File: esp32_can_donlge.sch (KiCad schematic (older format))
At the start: 0 parts

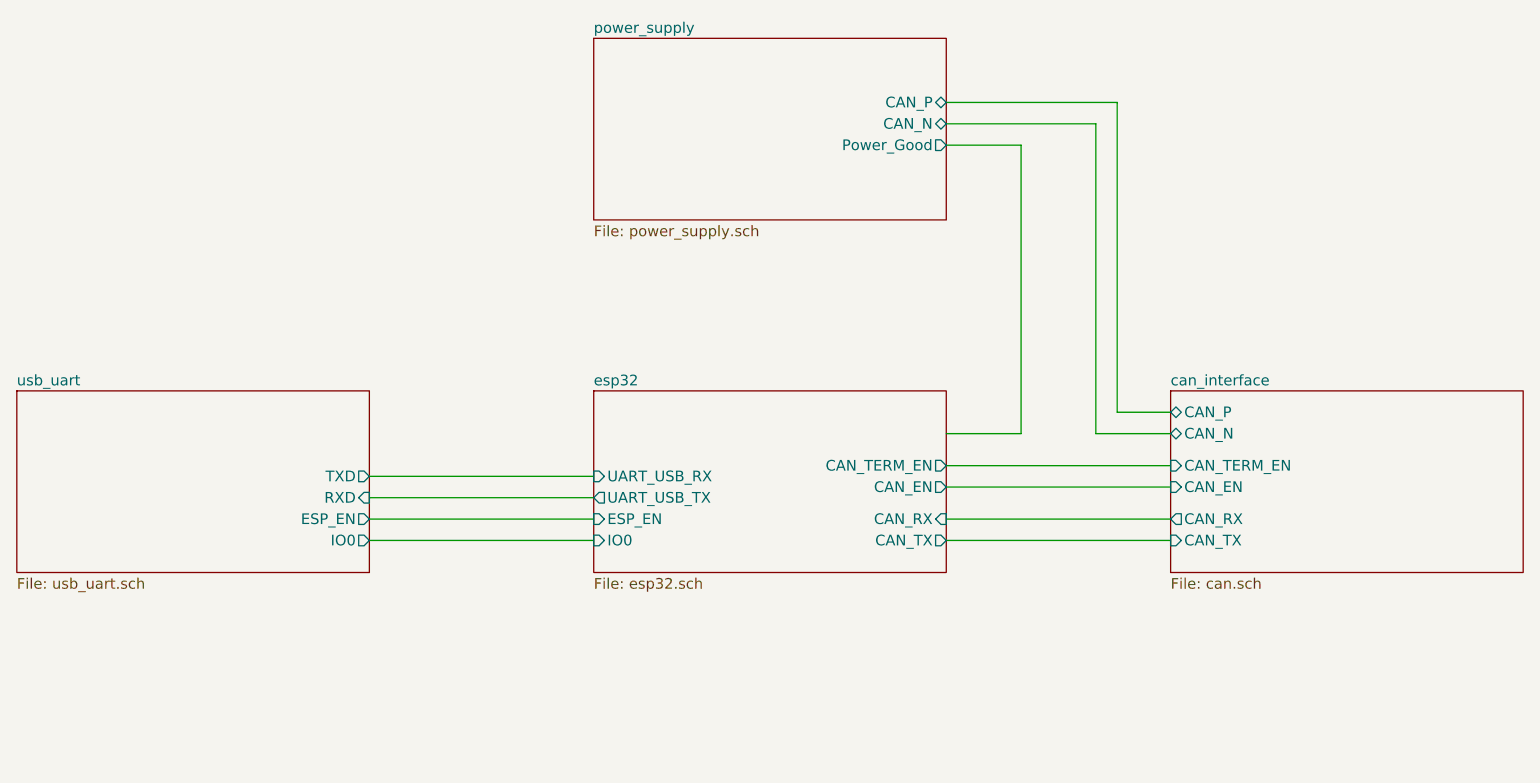
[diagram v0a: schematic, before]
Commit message: changed to a more basic variant of the esp32
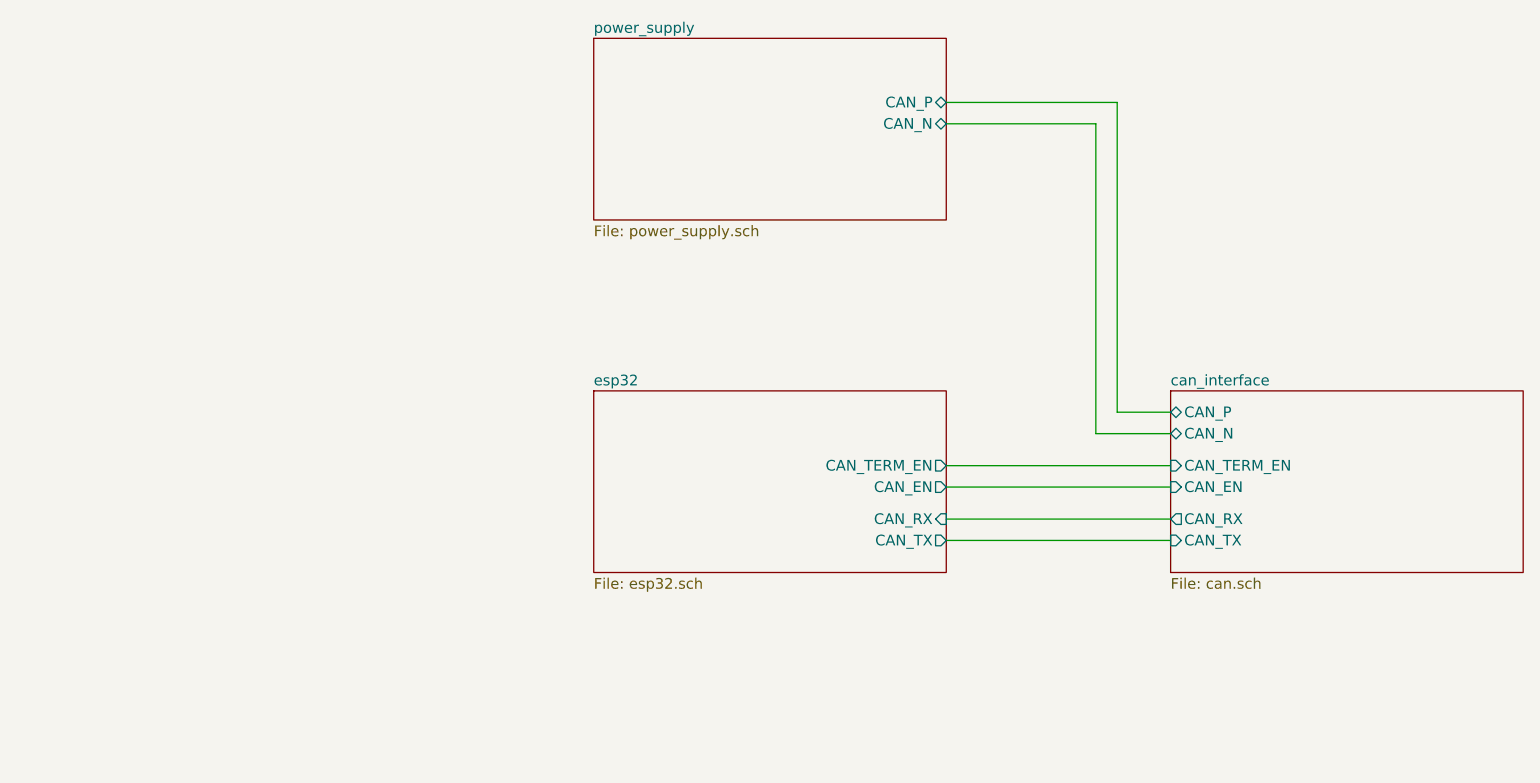
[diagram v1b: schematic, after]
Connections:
- wire segments 17 -> 10
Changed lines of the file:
@@
 $Descr A4 11693 8268
 encoding utf-8
-Sheet 1 5
-Title "WIFI-CAN-Dongle"
-Date "2018-09-30"
+Sheet 1 4
+Title "WIFI-CAN-Dongle Basic"
+Date "2018-10-03"
 Rev "v1.0"
 Comp "bytewerk - www.bytewerk.org"
-Comment1 "template author"
+Comment1 ""
 Comment2 "Stephan Hültl"
 Comment3 ""
@@
 F2 "CAN_RX" I R 6450 3700 50
 F3 "CAN_TX" O R 6450 3800 50
-F4 "UART_USB_TX" O L 4800 3600 50
-F5 "UART_USB_RX" I L 4800 3500 50
 F6 "CAN_EN" O R 6450 3550 50
 F7 "CAN_TERM_EN" O R 6450 3450 50
-F8 "ESP_EN" I L 4800 3700 50
-F9 "IO0" I L 4800 3800 50
 $EndSheet
 $Sheet
@@
 F2 "CAN_P" B R 6450 1750 50
 F3 "CAN_N" B R 6450 1850 50
-F4 "Power_Good" O R 6450 1950 50
-$EndSheet
-$Sheet
-S 2100 3100 1650 850
-U 5BAFF00B
-F0 "usb_uart" 50
-F1 "usb_uart.sch" 50
-F2 "RXD" I R 3750 3600 50
-F3 "TXD" O R 3750 3500 50
-F4 "ESP_EN" O R 3750 3700 50
-F5 "IO0" O R 3750 3800 50
 $EndSheet
 Wire Wire Line
@@
 Wire Wire Line
 	6450 3450 7500 3450
-Wire Wire Line
-	3750 3500 4800 3500
-Wire Wire Line
-	4800 3600 3750 3600
-Wire Wire Line
-	3750 3700 4800 3700
-Wire Wire Line
-	3750 3800 4800 3800
-Wire Wire Line
-	6450 1950 6800 1950
-Wire Wire Line
-	6800 1950 6800 3300
-Wire Wire Line
-	6800 3300 6450 3300
 $EndSCHEMATC

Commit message: minor changes in schematic, fixed wrong footprint of voltage regulator
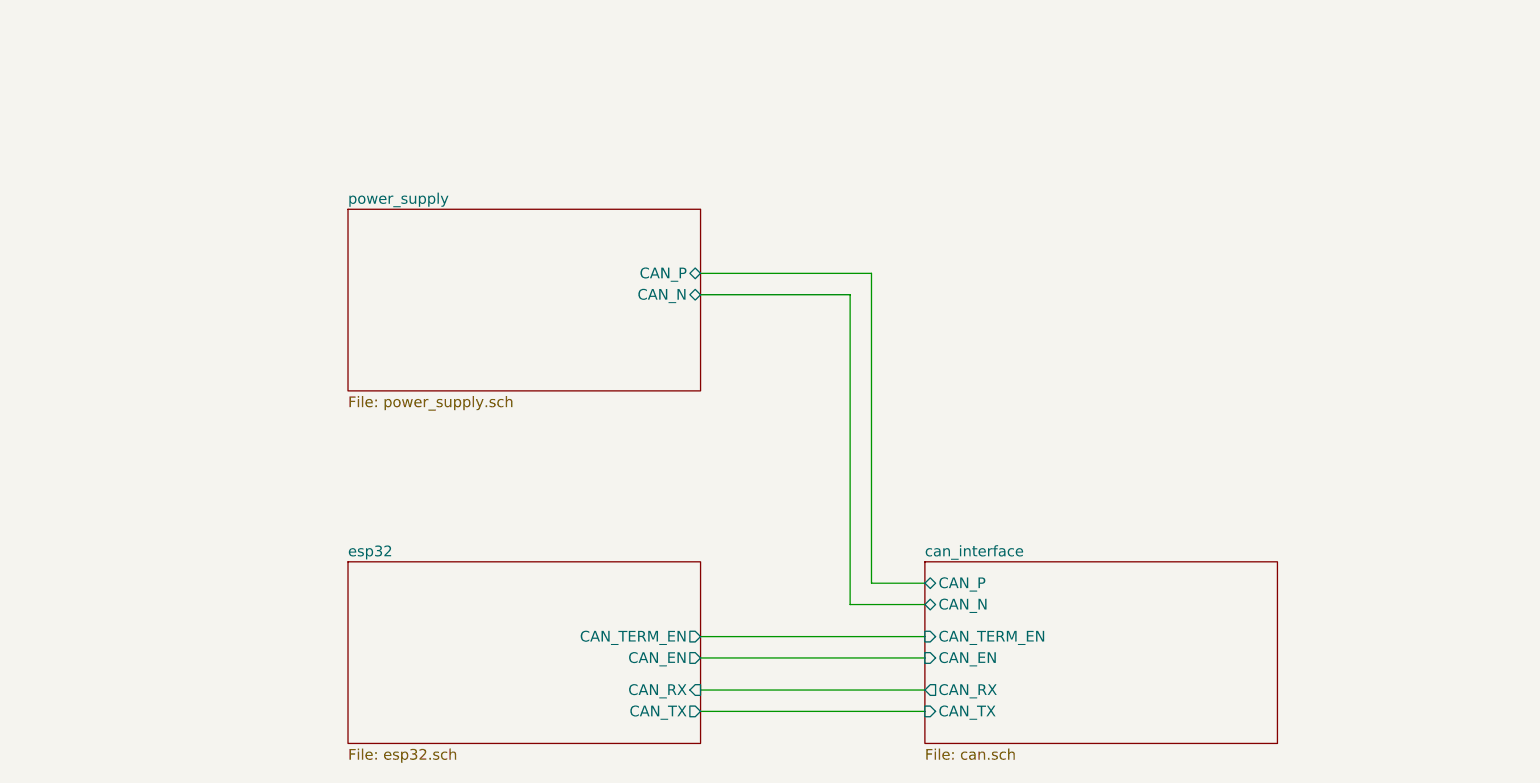
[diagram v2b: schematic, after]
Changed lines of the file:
@@
 $EndDescr
 $Sheet
-S 4800 3100 1650 850
+S 3650 3900 1650 850
 U 5BAFEFFB
 F0 "esp32" 50
 F1 "esp32.sch" 50
-F2 "CAN_RX" I R 6450 3700 50
-F3 "CAN_TX" O R 6450 3800 50
-F6 "CAN_EN" O R 6450 3550 50
-F7 "CAN_TERM_EN" O R 6450 3450 50
+F2 "CAN_RX" I R 5300 4500 50
+F3 "CAN_TX" O R 5300 4600 50
+F4 "CAN_EN" O R 5300 4350 50
+F5 "CAN_TERM_EN" O R 5300 4250 50
 $EndSheet
 $Sheet
-S 7500 3100 1650 850
+S 6350 3900 1650 850
 U 5BAFEFFE
 F0 "can_interface" 50
 F1 "can.sch" 50
-F2 "CAN_TX" I L 7500 3800 50
-F3 "CAN_RX" O L 7500 3700 50
-F4 "CAN_EN" I L 7500 3550 50
-F5 "CAN_P" B L 7500 3200 50
-F6 "CAN_TERM_EN" I L 7500 3450 50
-F7 "CAN_N" B L 7500 3300 50
+F2 "CAN_TX" I L 6350 4600 50
+F3 "CAN_RX" O L 6350 4500 50
+F4 "CAN_EN" I L 6350 4350 50
+F5 "CAN_P" B L 6350 4000 50
+F6 "CAN_TERM_EN" I L 6350 4250 50
+F7 "CAN_N" B L 6350 4100 50
 $EndSheet
 $Sheet
-S 4800 1450 1650 850
+S 3650 2250 1650 850
 U 5BAFF001
 F0 "power_supply" 50
 F1 "power_supply.sch" 50
-F2 "CAN_P" B R 6450 1750 50
-F3 "CAN_N" B R 6450 1850 50
+F2 "CAN_P" B R 5300 2550 50
+F3 "CAN_N" B R 5300 2650 50
 $EndSheet
 Wire Wire Line
-	6450 3700 7500 3700
+	5300 4500 6350 4500
 Wire Wire Line
-	7500 3800 6450 3800
+	6350 4600 5300 4600
 Wire Wire Line
-	7500 3200 7250 3200
+	6350 4000 6100 4000
 Wire Wire Line
-	7250 3200 7250 1750
+	6100 4000 6100 2550
 Wire Wire Line
-	7250 1750 6450 1750
+	6100 2550 5300 2550
 Wire Wire Line
-	6450 1850 7150 1850
+	5300 2650 6000 2650
 Wire Wire Line
-	7150 1850 7150 3300
+	6000 2650 6000 4100
 Wire Wire Line
-	7150 3300 7500 3300
+	6000 4100 6350 4100
 Wire Wire Line
-	6450 3550 7500 3550
+	5300 4350 6350 4350
 Wire Wire Line
-	6450 3450 7500 3450
+	5300 4250 6350 4250
 $EndSCHEMATC
